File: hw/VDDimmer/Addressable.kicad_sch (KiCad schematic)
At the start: 18 parts, among them J10 A2 V+SEL VIN/5V, J7 ADDR1 V+/D/CLK/GND, J8 ADDR2 V+/D/CLK/GND, J9 A1 V+SEL VIN/5V, U5 74HCT125

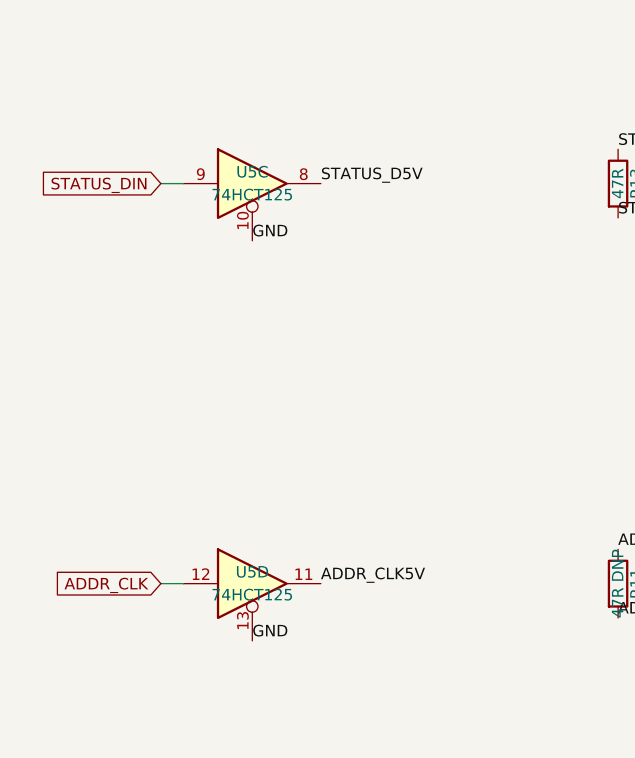
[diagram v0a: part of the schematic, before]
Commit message: Route the addressable section; swap U5 ch3/ch4 and U1's CLK/STATUS pins
Two pin swaps were needed to make the section planar; both are functionally
free and neither changes the BOM:

1. U5 channels 3 and 4 exchanged (A3/Y3 <-> A4/Y4). Both OE pins are tied to
   GND, so the channels are interchangeable. Before the swap STATUS_D5V left
   pin 8 (y=118.41, the southern output) heading north to R13, while
   ADDR_CLK5V left pin 11 (y=114.6, northern) heading south to R11/R12 -- a
   forced crossing. After the swap each output leaves on the side its load is
   on.
2. U1's ADDR_CLK and STATUS_DIN exchanged (IO45 pad26 <-> IO48 pad25). The
   ch3/ch4 swap inverted the required order at U5's inputs; moving the two
   source pins restores north-source-to-north-pad ordering.

U5's four inputs descend the SOIC body gap on lanes x = 168.6/169.1/170.1/170.6
-- the same trick used on U4 -- which frees both pad columns for the outputs.

Re-placement: R9/R11 moved from the x 175..181 cluster to x 156.5/161.5 beside
J7, R10/R12 to x 173.5/177 beside J8, all at y=125.0; R13 to (177,117).
Previously all five sat 15-20 mm from the connectors they feed. C34 moved to
(172,90) to clear the STATUS_DIN lane at y=92.0 (was 0.025 mm).
PF1/PF2 rotated 180 so V+SEL faces J9/J10 (east) and VOUT faces the JSTs
(west); this turned two wrapping nets into single L-bends.

Bottom-layer copper: one 1.25 mm B.Cu hop on ADDR2_D5V at x=172.588, y
122.775..124.025 (two 0.6/0.3 mm vias), where it must cross the ADDR_CLK5V
bus that straddles it. ADDR_CLK5V feeds R11 (x=160.6) and R12 (x=176.1) with
R10's feed at x=172.6 between them, so one crossing is topologically forced.
The cut in the bottom GND pour is 1.25 x 0.6 mm at 78 mm from the buck; the
8.5.3 keepout region is untouched.

DRC 0 errors, 0 phantom pads, unconnected 166 -> 146.

Co-Authored-By: Claude Opus 5 (1M context) <noreply@anthropic.com>
Claude-Session: https://claude.ai/code/session_01XeXr1isxVCg8kRo5Eh8BHM
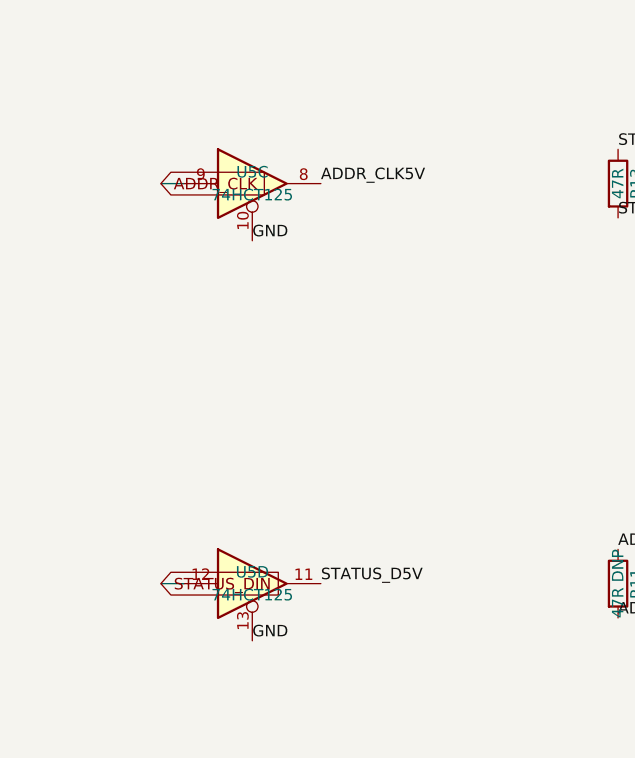
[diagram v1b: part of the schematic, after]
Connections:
- net ADDR_CLK: now also U5.9; no longer U5.12
- net ADDR_CLK5V: now also U5.8; no longer U5.11
- net STATUS_D5V: now also U5.11; no longer U5.8
- net STATUS_DIN: now also U5.12; no longer U5.9
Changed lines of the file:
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@@
-	)
-	(label "STATUS_D5V"
-		(at 67.31 160.02 0)
-		(effects
-			(font
-				(size 1.27 1.27)
-			)
-			(justify left bottom)
-		)
 	)
 	(label "STATUS_D5V"
@@
 	)
 	(label "ADDR_CLK5V"
-		(at 67.31 204.47 0)
-		(effects
-			(font
-				(size 1.27 1.27)
-			)
-			(justify left bottom)
-		)
-	)
-	(label "ADDR_CLK5V"
 		(at 100.33 200.66 0)
 		(effects
@@
 			)
 			(justify right bottom)
+		)
+	)
+	(label "ADDR_CLK5V"
+		(at 67.31 160.02 0)
+		(effects
+			(font
+				(size 1.27 1.27)
+			)
+			(justify left bottom)
+		)
+	)
+	(label "STATUS_D5V"
+		(at 67.31 204.47 0)
+		(effects
+			(font
+				(size 1.27 1.27)
+			)
+			(justify left bottom)
 		)
 	)
@@
 		)
 	)
-	(global_label "STATUS_DIN"
-		(shape input)
-		(at 49.53 160.02 180)
-		(effects
-			(font
-				(size 1.27 1.27)
-			)
-			(justify right)
-		)
-	)
-	(global_label "ADDR_CLK"
-		(shape input)
-		(at 49.53 204.47 180)
-		(effects
-			(font
-				(size 1.27 1.27)
-			)
-			(justify right)
-		)
-	)
 	(global_label "VIN_PROT"
 		(shape input)
@@
 		)
 	)
+	(global_label "ADDR_CLK"
+		(shape input)
+		(at 49.53 160.02 0)
+		(effects
+			(font
+				(size 1.27 1.27)
+			)
+			(justify left)
+		)
+	)
+	(global_label "STATUS_DIN"
+		(shape input)
+		(at 49.53 204.47 0)
+		(effects
+			(font
+				(size 1.27 1.27)
+			)
+			(justify left)
+		)
+	)
 	(symbol
 		(lib_id "74xx:74AHCT125")
@@
 			)
 		)
+		(property "Assembly" "DNP - APA102 clock provision per spec 6.2"
+			(at 100.33 204.47 0)
+			(hide yes)
+			(effects
+				(font
+					(size 1.27 1.27)
+				)
+			)
+		)
 		(instances
 			(project "Addressable"
@@
 			)
 		)
-		(property "Assembly" "DNP - APA102 clock provision per spec 6.2"
-			(at 100.33 204.47 0)
-			(hide yes)
-			(effects
-				(font
-					(size 1.27 1.27)
-				)
-			)
-		))
+	)
 	(symbol
 		(lib_id "Device:R")
@@
 			)
 		)
+		(property "Assembly" "DNP - APA102 clock provision per spec 6.2"
+			(at 129.54 204.47 0)
+			(hide yes)
+			(effects
+				(font
+					(size 1.27 1.27)
+				)
+			)
+		)
 		(instances
 			(project "Addressable"
@@
 			)
 		)
-		(property "Assembly" "DNP - APA102 clock provision per spec 6.2"
-			(at 129.54 204.47 0)
-			(hide yes)
-			(effects
-				(font
-					(size 1.27 1.27)
-				)
-			)
-		))
+	)
 	(symbol
 		(lib_id "Connector_Generic:Conn_01x03")

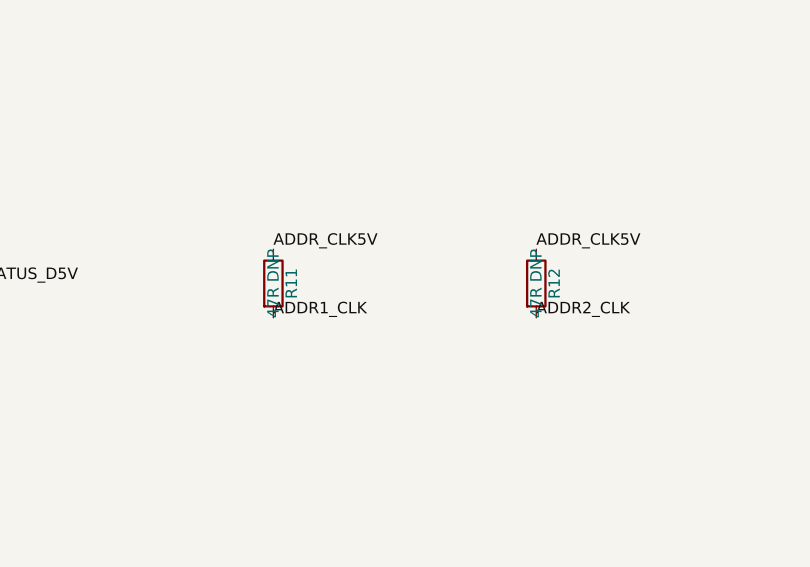
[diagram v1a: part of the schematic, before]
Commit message: Schematic pass: MPN/LCSC/Manufacturer on all 79 sourced parts
F1 -> "8A 250V", U3 -> "BL1117-33CX", J2 -> "VIN 12V" (was "VIN 9-24V",
which invited 24 V into an 18 V TVS). R11/R12 values cleaned to "47R" with
the DNP intent moved into the Assembly field. ERC still 0 violations.

Every sourced part now carries MPN, LCSC and Manufacturer, plus an Assembly
note anywhere the choice needs explaining - why D5 is an SMBJ18A, why R30's
current rating still needs checking, why L1 is candidate-only.

Two things this pass could NOT do, both because no MCP tool writes them:

- KiCad's (dnp yes) attribute. R11 and R12 must be flagged in the GUI; their
  Assembly fields say so. All five text-only DNPs were in this state, but
  L3/C20/R31 are now fitted by decision, so only R11/R12 remain.
- Fields on units 2-5 of a multi-unit symbol. Konnect writes unit 1 only,
  where the GUI propagates to all units. U4/U5 are 5-unit 74HCT125s, so
  grouping a BOM by MPN splits U5 into two lines and would order 3 of a
  2-off part. tools/export-bom.sh groups by Value+Footprint instead, which
  collapses correctly - 49 lines, 96 parts, and the 15 lines without an LCSC
  are exactly the mounting holes and hand-fit connectors.

Also checked and left alone: the U4/U5 symbol's lib_id is 74AHCT125 while its
value is 74HCT125. AHCT would be the conventional WS2812 level shifter, but
JLC has 70 of it in SO-14 against 88,003 of the HCT part, and HCT is fine here
- TTL inputs, 15 ns against 300 ns bit times. The value is the buyable intent.

Co-Authored-By: Claude Opus 5 (1M context) <noreply@anthropic.com>
Claude-Session: https://claude.ai/code/session_01QsYnM2qRBWQsyKPH1v7rLR
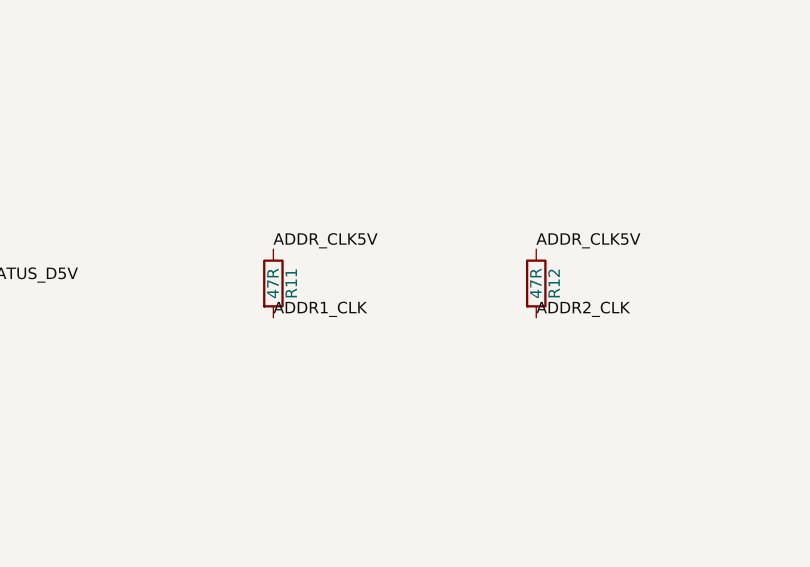
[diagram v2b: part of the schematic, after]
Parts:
- C60, C62: LCSC (none) -> C14663; MPN (none) -> CC0603KRX7R9BB104; Manufacturer (none) -> YAGEO
- C61: LCSC (none) -> C15850; MPN (none) -> CL21A106KAYNNNE; Manufacturer (none) -> Samsung Electro-Mechanics
- C63, C64: LCSC (none) -> C5156756; MPN (none) -> FS32X106K101EGG; Manufacturer (none) -> PSA
- D7: Assembly (none) -> SUBSTITUTE - the V6 revision is not in JLC's catalogue. Con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; LCSC (none) -> C2874885; MPN (none) -> WS2812B-V5/W; Manufacturer (none) -> Worldsemi
- PF1, PF2: LCSC (none) -> C18198342; MPN (none) -> 1812L200/30GR; Manufacturer (none) -> LUTE
- R10, R13, R9: LCSC (none) -> C17714; MPN (none) -> 0805W8F470JT5E; Manufacturer (none) -> UNI-ROYAL
- R11, R12: value 47R DNP -> 47R; Assembly DNP - APA102 clock provision per spec 6.2 -> DNP - APA102 clock provision per spec 6.2. Needs KiCad's (d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; LCSC (none) -> C17714; MPN (none) -> 0805W8F470JT5E; Manufacturer (none) -> UNI-ROYAL
- U5: LCSC (none) -> C5962; MPN (none) -> 74HCT125D,653; Manufacturer (none) -> Nexperia

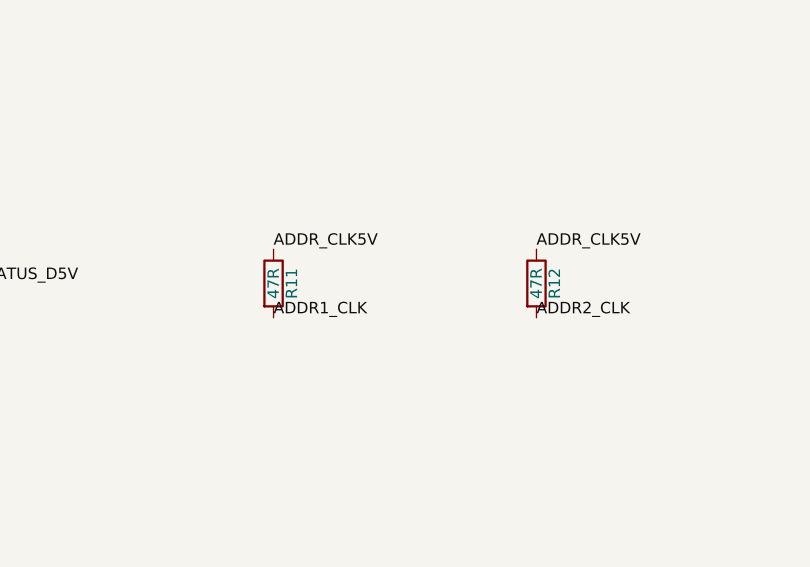
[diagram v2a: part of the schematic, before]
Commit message: Fix six drill defects, fit the I2C pull-ups, add the board ID
Drill defects
-------------
hole_to_hole and holes_co_located are downgraded to warning in .kicad_pro, so
the board reported "DRC 0 errors" while carrying five hole_to_hole and one
holes_co_located -- two of them with physically overlapping drills. Same shape
of trap as the split-net lesson already in HANDOFF.

Five vias deleted, each proven non-load-bearing first by checking which track
endpoints actually land on it. In every overlapping pair only one via carried a
track; the other was a bare stitching via with its twin 0.1-0.5 mm away.
d85c5d26 was redundant by construction -- 1 mm from J2's PTH GND pad, which
already ties both layers. afb88017 was an exact duplicate of a14092cd.
Afterwards GND is still one connected group, the split-net count is unchanged
at 12, and via count went 192 -> 187.

I2C pull-ups (R45, R46)
-----------------------
4.7k 0805, C17673, per the 2026-08-29 decision. Verified against the exported
netlist rather than the tools' return values, because the pins are tied with a
plain +3V3 net label -- the convention J13's own supply pin uses on this sheet.
Had that not merged with the power net the pull-ups would have pulled to
nothing, which is the silent failure the decision existed to prevent.

  +3V3          15 nodes  ... J13.1 R43.1 R44.1 R45.1 R46.1 U1.2 U3.2
  /MCU/I2C_SDA   3 nodes  J13.3  R45.2  U1.20
  /MCU/I2C_SCL   3 nodes  J13.4  R46.2  U1.18

The taps run on B.Cu because ADDR1_DIN crosses the whole board on F.Cu at
y=96.33, x 149.35-168.60, walling +3V3 (which reaches J13.1 at y=95) off from
the I2C lines at y=100.14 and 102.67. There is no F.Cu-only path; going round
its east end costs ~30 mm and still needs via hops over the GATE_IN verticals.
B.Cu there is bare GND pour and J13's pads 1/3/4 are through-hole, so they are
reachable from below with no via at that end.

Both parts are rotated 180 deg. They arrive with pad 1 (+3V3) west, which would
force the SDA return to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
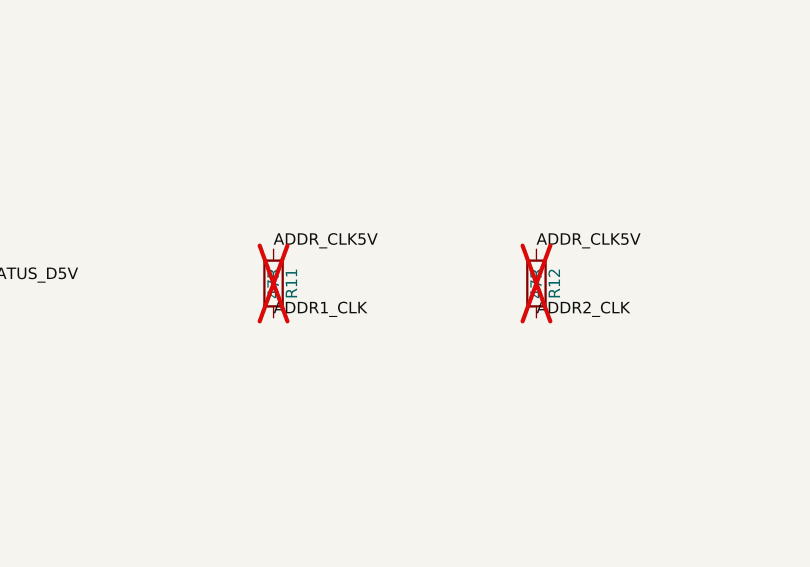
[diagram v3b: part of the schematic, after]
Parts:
- R11, R12: now not fitted
- U5: LCSC (none) -> C5962; MPN (none) -> 74HCT125D,653; Manufacturer (none) -> Nexperia

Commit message: Swap the five 10uF 1210s from 100 V to 50 V: -$1.44/board
The board carried FS32X106K101EGG (C5156756), a 100 V 1210, at $0.4774 -- five
per board, 20% of the whole BOM, on a board that is 12 V only. Replaced with
HGC1210R7106M500NSVK (C33546018), 10uF 50V X7R +/-20%, $0.1901, stock 16809.

  component cost   $11.886 -> $10.450 per board   (saving $1.44)

Voltage margin checked rather than assumed. All five sit on 12 V-class rails:

  C20        VIN_DAMP            input LC filter
  C21, C22   VIN_BUCK            buck input capacitors
  C63, C64   ADDR1/2_VOUT        switchable 12 V or 5 V via J9/J10

and D5, the SMBJ18A, clamps input transients at 29.2 V -- comfortably under the
50 V rating. The 1210 land is unchanged; both parts share the same EasyEDA
footprint UUID.

Deliberately NOT the 25 V part (C39232, $0.1303, a further $0.30/board): C21/C22
are the buck's input capacitors and a 25 V X7R 1210 loses 40-60% of its
capacitance at 12 V DC bias. At 50 V with +/-20% tolerance the pair still gives
roughly 13-14 uF effective, against the AP63301's ~10 uF want.

Incidental tidy-up: the schematic Values already read "10uF/50V", so the 100 V
part was the one out of step. They now agree.

Leaves schematic parity at 5 -- the LCSC field differs between schematic and
board footprint for these five caps. Cosmetic; BOM and CPL are generated from
the schematic, so the fab data is correct. One F8 sync clears it.

ERC 0, DRC 0 errors, 165 warnings, 15 unconnected. JLC bundle regenerated.

Co-Authored-By: Claude Opus 5 (1M context) <noreply@anthropic.com>
Claude-Session: https://claude.ai/code/session_01AnYUdWpnpbT2cnPRPqtfVa
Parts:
- C63, C64: LCSC C5156756 -> C33546018; MPN FS32X106K101EGG -> HGC1210R7106M500NSVK; Manufacturer PSA -> Chinocera
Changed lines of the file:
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@@
 			)
 		)
-		(property "LCSC" "C5156756"
+		(property "LCSC" "C33546018"
 			(at 275.59 69.85 0)
 			(hide yes)
@@
 			)
 		)
-		(property "MPN" "FS32X106K101EGG"
+		(property "MPN" "HGC1210R7106M500NSVK"
 			(at 275.59 69.85 0)
 			(hide yes)
@@
 			)
 		)
-		(property "Manufacturer" "PSA"
+		(property "Manufacturer" "Chinocera"
 			(at 275.59 69.85 0)
 			(hide yes)
@@
 			)
 		)
-		(property "LCSC" "C5156756"
+		(property "LCSC" "C33546018"
 			(at 275.59 129.54 0)
 			(hide yes)
@@
 			)
 		)
-		(property "MPN" "FS32X106K101EGG"
+		(property "MPN" "HGC1210R7106M500NSVK"
 			(at 275.59 129.54 0)
 			(hide yes)
@@
 			)
 		)
-		(property "Manufacturer" "PSA"
+		(property "Manufacturer" "Chinocera"
 			(at 275.59 129.54 0)
 			(hide yes)

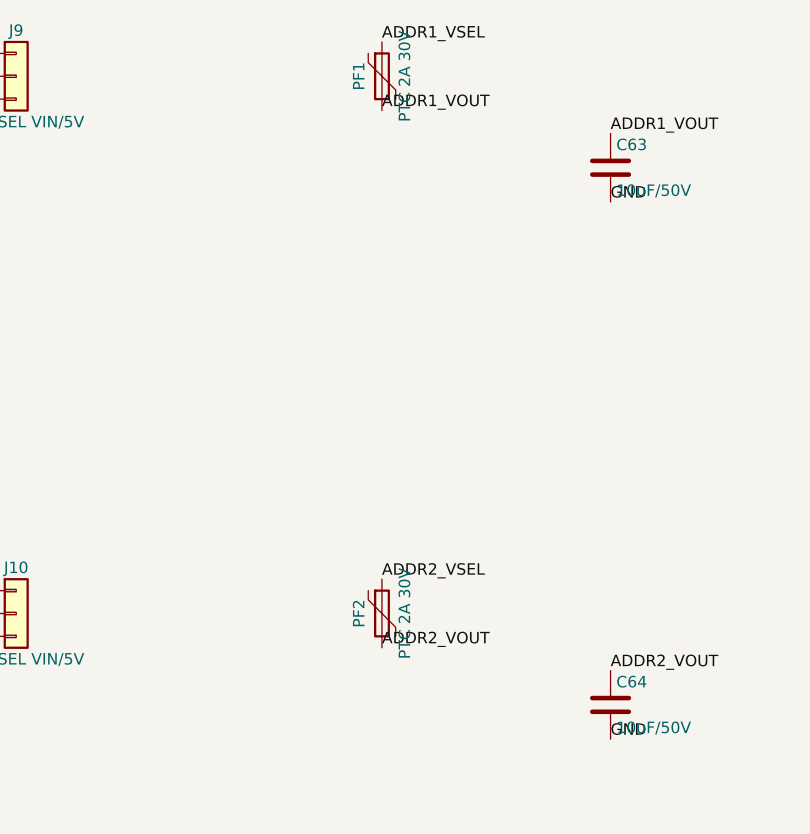
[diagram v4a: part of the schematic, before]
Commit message: Re-rate PF1/PF2 to 3 A; 1.7 A against a 2 A hold nuisance-trips warm
WS2815 at 12 V draws ~1.7 A per addressable output, and polyfuse hold
current derates with ambient temperature, so the 2 A parts would nuisance-
trip in a warm enclosure.

LUTE 1812L300/30GR (C48985875): 3 A hold / 5 A trip / 30 V, same 1812 land.
30 V is retained -- these sit downstream of the jumper and may see VIN_PROT.

Chosen over the 33 V (C54300298, 6.8k stock) and BNstar (C47002391, 5.5k)
alternatives because it is the same LUTE 1812L series as the outgoing part
and carries the SAME EasyEDA footprint UUID ab17c647a0a943b09958724a36a719c7,
so it is an assembly part rather than catalogue-only -- the failure mode that
already cost F1 a part swap.

Co-Authored-By: Claude Opus 5 (1M context) <noreply@anthropic.com>
Claude-Session: https://claude.ai/code/session_01YZHVU8aymL4RkLeCfwomwj
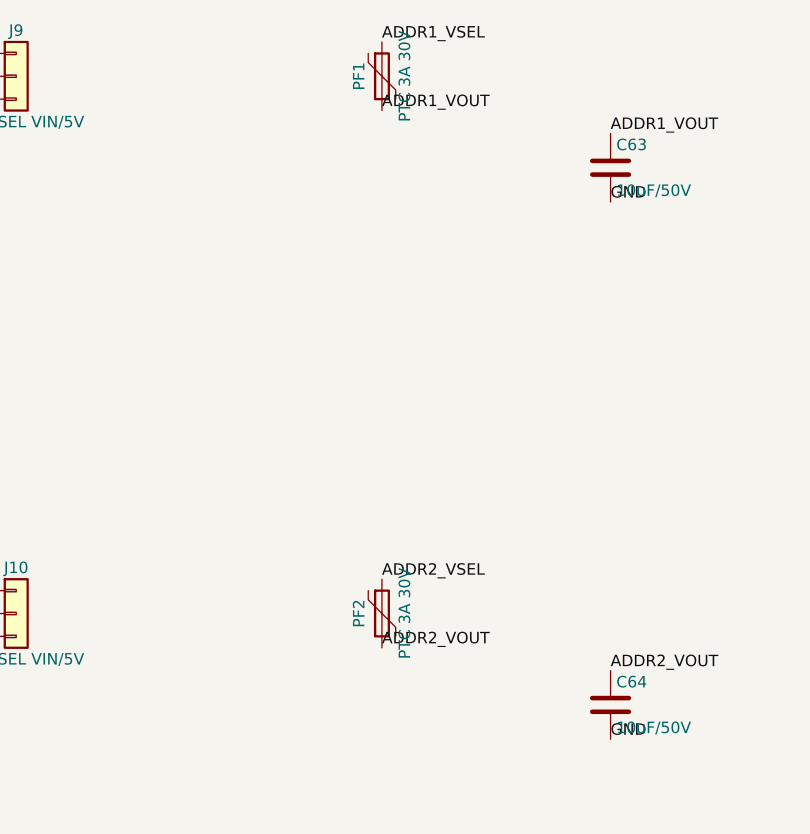
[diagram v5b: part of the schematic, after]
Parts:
- PF1, PF2: value PTC 2A 30V -> PTC 3A 30V; LCSC C18198342 -> C48985875; MPN 1812L200/30GR -> 1812L300/30GR
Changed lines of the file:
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@@
 			)
 		)
-		(property "Value" "PTC 2A 30V"
+		(property "Value" "PTC 3A 30V"
 			(at 252.73 59.69 90)
 			(show_name no)
@@
 			)
 		)
-		(property "LCSC" "C18198342"
+		(property "LCSC" "C48985875"
 			(at 250.19 59.69 0)
 			(hide yes)
@@
 			)
 		)
-		(property "MPN" "1812L200/30GR"
+		(property "MPN" "1812L300/30GR"
 			(at 250.19 59.69 0)
 			(hide yes)
@@
 			)
 		)
-		(property "Value" "PTC 2A 30V"
+		(property "Value" "PTC 3A 30V"
 			(at 252.73 119.38 90)
 			(show_name no)
@@
 			)
 		)
-		(property "LCSC" "C18198342"
+		(property "LCSC" "C48985875"
 			(at 250.19 119.38 0)
 			(hide yes)
@@
 			)
 		)
-		(property "MPN" "1812L200/30GR"
+		(property "MPN" "1812L300/30GR"
 			(at 250.19 119.38 0)
 			(hide yes)
